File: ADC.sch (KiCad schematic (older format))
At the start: 4 parts, among them U5 MAX11128

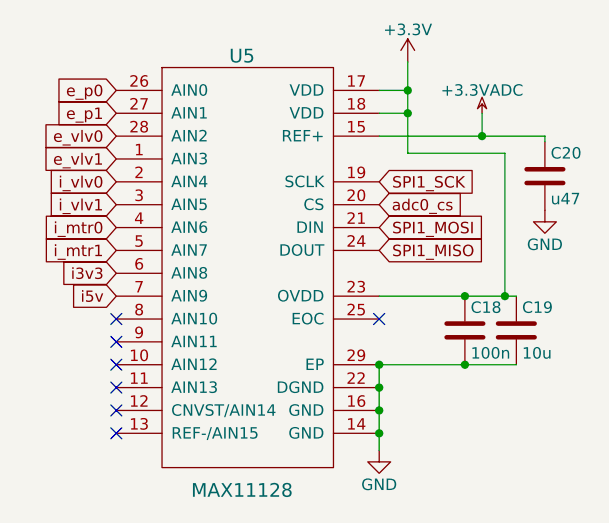
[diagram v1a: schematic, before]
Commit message: Motor Channel Cleanup
Removed some leftover labels in the motor channel after removal of the AND gate. Renumbering.
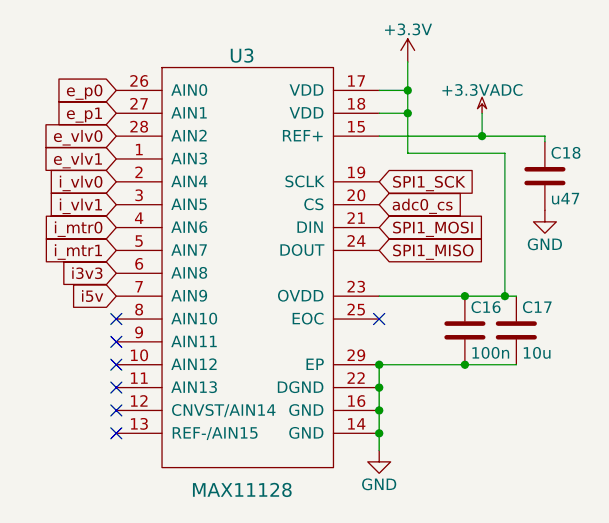
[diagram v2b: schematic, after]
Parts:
- renumbered C18 to C16, C19 to C17, C20 to C18, U5 to U3
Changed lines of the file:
@@
 AR Path="/596D7A67/5C1804A3/5E64F4D7" Ref="U?"  Part="1"
 AR Path="/5E49E893/5E64F4D7" Ref="U?"  Part="1"
-AR Path="/5E63996E/5E64F4D7" Ref="U5"  Part="1"
-F 0 "U5" H 5325 3850 60  0000 C CNN
+AR Path="/5E63996E/5E64F4D7" Ref="U3"  Part="1"
+F 0 "U3" H 5325 3850 60  0000 C CNN
 F 1 "MAX11128" H 5325 1950 60  0000 C CNN
 F 2 "sternie:TQFN-28" H 4775 3400 60  0001 C CNN
@@
 AR Path="/596D7A67/5C1804A3/5E64F4DD" Ref="#PWR?"  Part="1"
 AR Path="/5E49E893/5E64F4DD" Ref="#PWR?"  Part="1"
-AR Path="/5E63996E/5E64F4DD" Ref="#PWR050"  Part="1"
-F 0 "#PWR050" H 6525 2450 50  0001 C CNN
+AR Path="/5E63996E/5E64F4DD" Ref="#PWR024"  Part="1"
+F 0 "#PWR024" H 6525 2450 50  0001 C CNN
 F 1 "+3.3VADC" H 6375 2600 50  0000 C CNN
 F 2 "" H 6375 2500 50  0001 C CNN
@@
 AR Path="/596D7A67/5C1804A3/5E64F4E3" Ref="#PWR?"  Part="1"
 AR Path="/5E49E893/5E64F4E3" Ref="#PWR?"  Part="1"
-AR Path="/5E63996E/5E64F4E3" Ref="#PWR049"  Part="1"
-F 0 "#PWR049" H 6050 2125 50  0001 C CNN
+AR Path="/5E63996E/5E64F4E3" Ref="#PWR023"  Part="1"
+F 0 "#PWR023" H 6050 2125 50  0001 C CNN
 F 1 "+3.3V" H 6050 2415 50  0000 C CNN
 F 2 "" H 6050 2275 50  0001 C CNN
@@
 AR Path="/596D7A67/5C1804A3/5E64F4E9" Ref="C?"  Part="1"
 AR Path="/5E49E893/5E64F4E9" Ref="C?"  Part="1"
-AR Path="/5E63996E/5E64F4E9" Ref="C20"  Part="1"
-F 0 "C20" H 6675 2875 50  0000 L CNN
+AR Path="/5E63996E/5E64F4E9" Ref="C18"  Part="1"
+F 0 "C18" H 6675 2875 50  0000 L CNN
 F 1 "u47" H 6675 2675 50  0000 L CNN
 F 2 "Capacitors_SMD:C_0603" H 6688 2625 50  0001 C CNN
@@
 AR Path="/596D7A67/5C1804A3/5E64F4EF" Ref="#PWR?"  Part="1"
 AR Path="/5E49E893/5E64F4EF" Ref="#PWR?"  Part="1"
-AR Path="/5E63996E/5E64F4EF" Ref="#PWR051"  Part="1"
-F 0 "#PWR051" H 6650 2675 50  0001 C CNN
+AR Path="/5E63996E/5E64F4EF" Ref="#PWR025"  Part="1"
+F 0 "#PWR025" H 6650 2675 50  0001 C CNN
 F 1 "GND" H 6650 2775 50  0000 C CNN
 F 2 "" H 6650 2925 50  0001 C CNN
@@
 AR Path="/596D7A67/5C1804A3/5E64F4F5" Ref="#PWR?"  Part="1"
 AR Path="/5E49E893/5E64F4F5" Ref="#PWR?"  Part="1"
-AR Path="/5E63996E/5E64F4F5" Ref="#PWR048"  Part="1"
-F 0 "#PWR048" H 5925 3725 50  0001 C CNN
+AR Path="/5E63996E/5E64F4F5" Ref="#PWR022"  Part="1"
+F 0 "#PWR022" H 5925 3725 50  0001 C CNN
 F 1 "GND" H 5925 3825 50  0000 C CNN
 F 2 "" H 5925 3975 50  0001 C CNN
@@
 AR Path="/596D7A67/5C1804A3/5E64F4FB" Ref="C?"  Part="1"
 AR Path="/5E49E893/5E64F4FB" Ref="C?"  Part="1"
-AR Path="/5E63996E/5E64F4FB" Ref="C18"  Part="1"
-F 0 "C18" H 6325 3550 50  0000 L CNN
+AR Path="/5E63996E/5E64F4FB" Ref="C16"  Part="1"
+F 0 "C16" H 6325 3550 50  0000 L CNN
 F 1 "100n" H 6325 3350 50  0000 L CNN
 F 2 "Capacitors_SMD:C_0603" H 6338 3300 50  0001 C CNN
@@
 AR Path="/596D7A67/5C1804A3/5E64F501" Ref="C?"  Part="1"
 AR Path="/5E49E893/5E64F501" Ref="C?"  Part="1"
-AR Path="/5E63996E/5E64F501" Ref="C19"  Part="1"
-F 0 "C19" H 6550 3550 50  0000 L CNN
+AR Path="/5E63996E/5E64F501" Ref="C17"  Part="1"
+F 0 "C17" H 6550 3550 50  0000 L CNN
 F 1 "10u" H 6550 3350 50  0000 L CNN
 F 2 "Capacitors_SMD:C_0805" H 6563 3300 50  0001 C CNN
